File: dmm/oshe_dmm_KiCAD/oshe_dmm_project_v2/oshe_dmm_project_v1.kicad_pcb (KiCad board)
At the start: 4 copper layers, 88.7 x 165.1 mm, 99 parts, among them J1 FTDI Basic, J10 Voltage Range 2, J11 Voltage Range 3, J12 Voltage Range 3, J13 DC Current Indication, J14 Continuity, J16 AC Voltage Range 2, J18 AC Voltage Range 3, J2 Voltage, J20 AC Voltage Range 1, J21 AC Current Indication, J22 MJ-3536N, J3 GND, J4 Current, J5 Resistance Meas, J6 ON/OFF, J7 Voltage Range 1, J8 Voltage Range 1, J9 Voltage Range 2, SW1 PTS526 SK15 SMTR2 LFS, U1 ATmega328P-A, U2 AD736, U3 ADS1115IDGS, U4 MAX4617CPE, U5 LM317_SOT-223, U7 TPS60400DBV, U8 ADS1115IDGS, Y1 16MHz

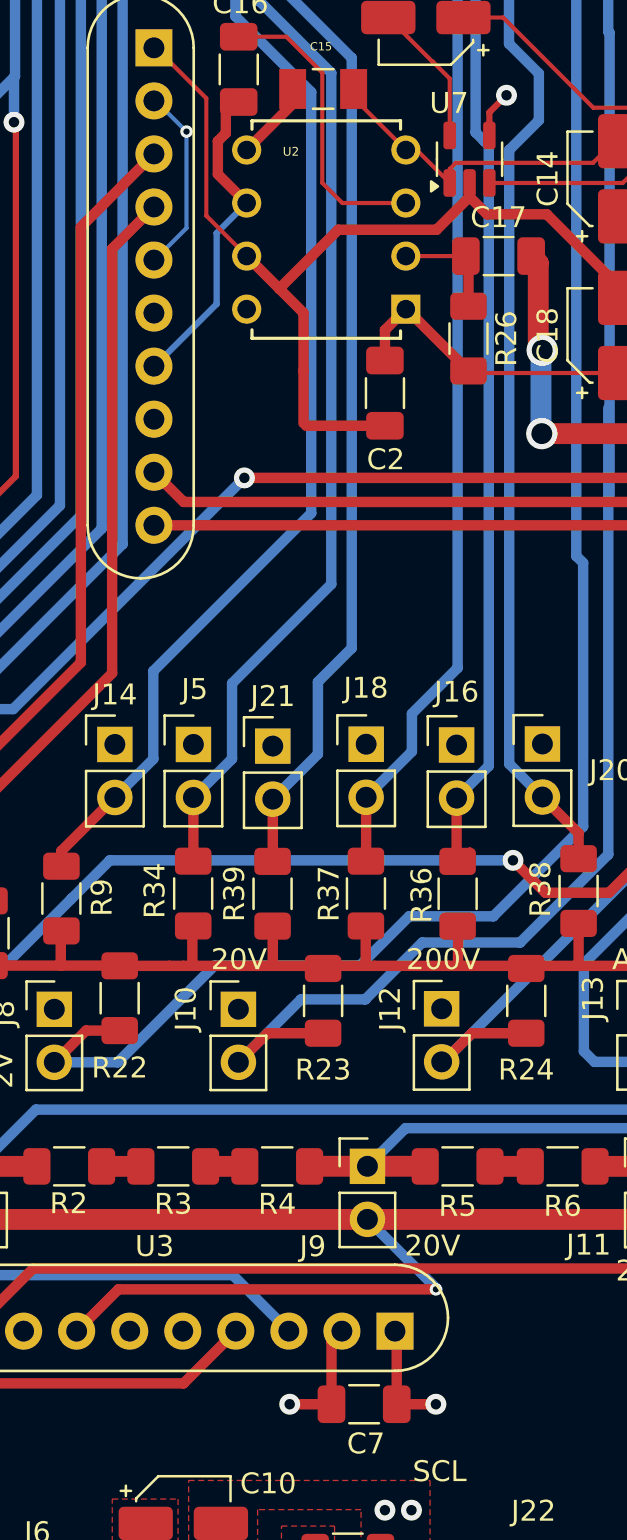
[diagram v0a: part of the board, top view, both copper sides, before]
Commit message: Removed buried vias
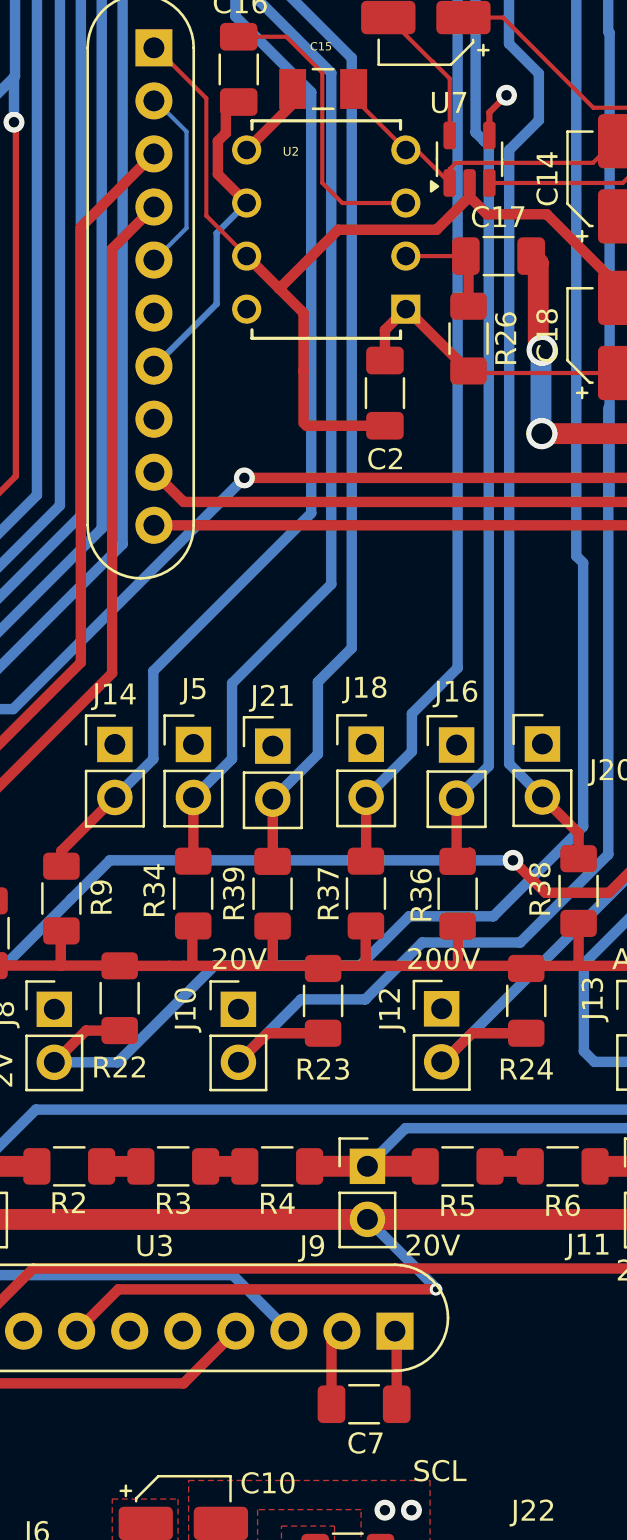
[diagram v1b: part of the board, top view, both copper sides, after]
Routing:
- net GND: track 88.7 -> 86.7 mm, vias 25 -> 23
- net +5V: track 162.8 -> 160.9 mm, vias 19 -> 18
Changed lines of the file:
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@@
-	)
-	(segment
-		(start 162.09 202.378)
-		(end 164.09 202.378)
-		(width 0.5)
-		(layer "F.Cu")
-		(net 2)
 	)
 	(segment
@@
 		(net 2)
 	)
-	(via blind
-		(at 162.09 202.378)
-		(size 1)
-		(drill 0.5)
-		(layers "F.Cu" "In1.Cu")
-		(free yes)
-		(net 2)
-	)
 	(via
 		(at 167.919 207.45)
@@
 		(net 2)
 	)
-	(via blind
-		(at 157.15 141.448)
-		(size 0.6)
-		(drill 0.3)
-		(layers "In1.Cu" "B.Cu")
-		(net 2)
-	)
 	(segment
 		(start 133.286 181.0106)
@@
 		(start 162.75 150.128)
 		(end 161.59 148.968)
-		(width 0.5)
-		(layer "F.Cu")
-		(net 4)
-	)
-	(segment
-		(start 169.09 202.378)
-		(end 167.215 202.378)
 		(width 0.5)
 		(layer "F.Cu")
@@
 		(free yes)
 		(net 4)
-	)
-	(via micro
-		(at 169.09 202.378)
-		(size 1)
-		(drill 0.5)
-		(layers "F.Cu" "In2.Cu")
-		(free yes)
-		(net 4)

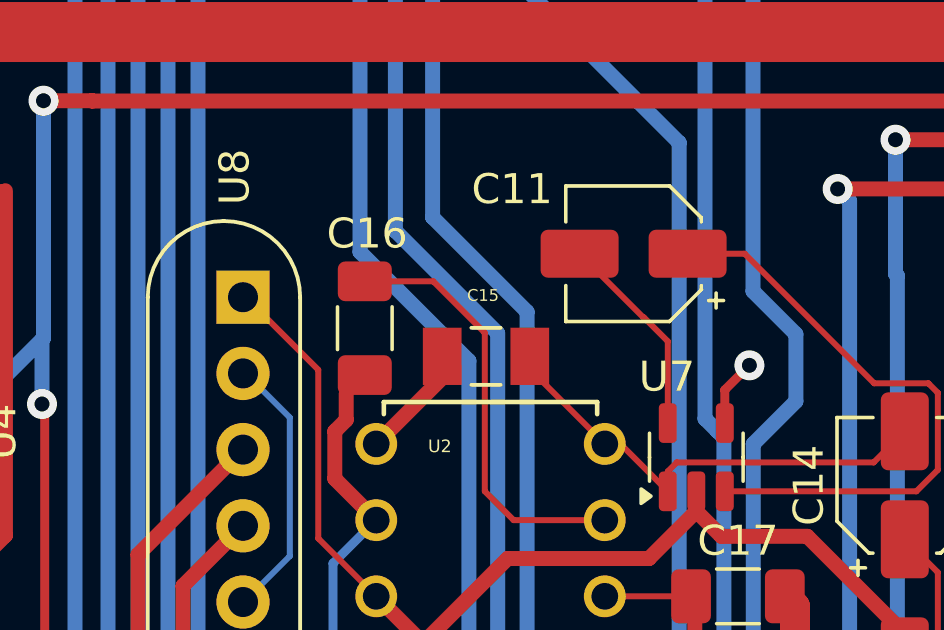
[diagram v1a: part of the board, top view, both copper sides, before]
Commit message: Removed a via
Removed a via that was incorrectly attached to multiple layers.
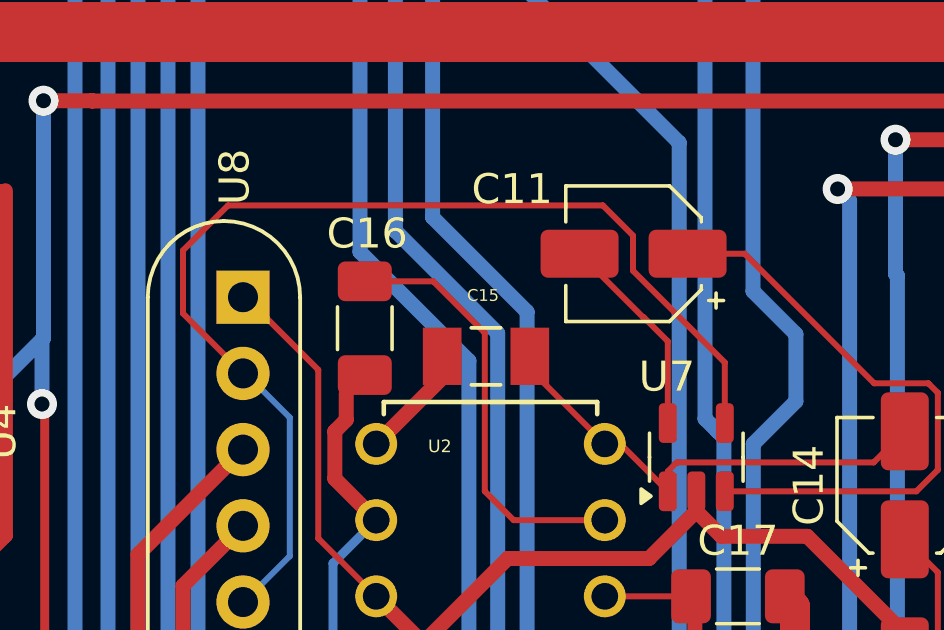
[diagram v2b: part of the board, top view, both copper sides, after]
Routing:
- net GND: track 86.7 -> 112.9 mm, vias 23 -> 22
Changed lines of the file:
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@@
+	)
+	(segment
+		(start 168.59 135.38184)
+		(end 167.58616 134.378)
+		(width 0.2)
+		(layer "F.Cu")
+		(net 2)
 	)
 	(segment
@@
 	)
 	(segment
+		(start 155.09 134.378)
+		(end 153.59 135.878)
+		(width 0.2)
+		(layer "F.Cu")
+		(net 2)
+	)
+	(segment
 		(start 133.286 172.5106)
 		(end 133.286 173.9476)
@@
 	)
 	(segment
+		(start 171.65 141.633)
+		(end 171.65 139.61416)
+		(width 0.2)
+		(layer "F.Cu")
+		(net 2)
+	)
+	(segment
+		(start 153.59 135.878)
+		(end 153.59 137.978)
+		(width 0.2)
+		(layer "F.Cu")
+		(net 2)
+	)
+	(segment
 		(start 135.699054 167.356146)
 		(end 135.699054 167.356054)
@@
 	)
 	(segment
-		(start 171.65 141.633)
-		(end 171.65 140.528)
-		(width 0.3)
-		(layer "F.Cu")
-		(net 2)
-	)
-	(segment
 		(start 127.2362 190.5378)
 		(end 126.144 191.63)
@@
 	)
 	(segment
-		(start 171.65 140.528)
-		(end 172.47 139.708)
-		(width 0.3)
-		(layer "F.Cu")
-		(net 2)
-	)
-	(segment
 		(start 134.067 174.7286)
 		(end 134.067 178.9196)
@@
 	)
 	(segment
+		(start 171.65 139.61416)
+		(end 168.59 136.55416)
+		(width 0.2)
+		(layer "F.Cu")
+		(net 2)
+	)
+	(segment
+		(start 168.59 136.55416)
+		(end 168.59 135.38184)
+		(width 0.2)
+		(layer "F.Cu")
+		(net 2)
+	)
+	(segment
 		(start 134.067 178.9196)
 		(end 134.086 178.9386)
@@
 	)
 	(segment
+		(start 167.58616 134.378)
+		(end 155.09 134.378)
+		(width 0.2)
+		(layer "F.Cu")
+		(net 2)
+	)
+	(segment
 		(start 177.65 153.008)
 		(end 170.75 153.008)
@@
 		(end 135.083 184.6346)
 		(width 0.3)
+		(layer "F.Cu")
+		(net 2)
+	)
+	(segment
+		(start 153.59 137.978)
+		(end 155.59 139.978)
+		(width 0.2)
 		(layer "F.Cu")
 		(net 2)
@@
 		(net 2)
 	)
-	(via
-		(at 172.47 139.708)
-		(size 1)
-		(drill 0.5)
-		(layers "F.Cu" "B.Cu")
-		(net 2)
-	)

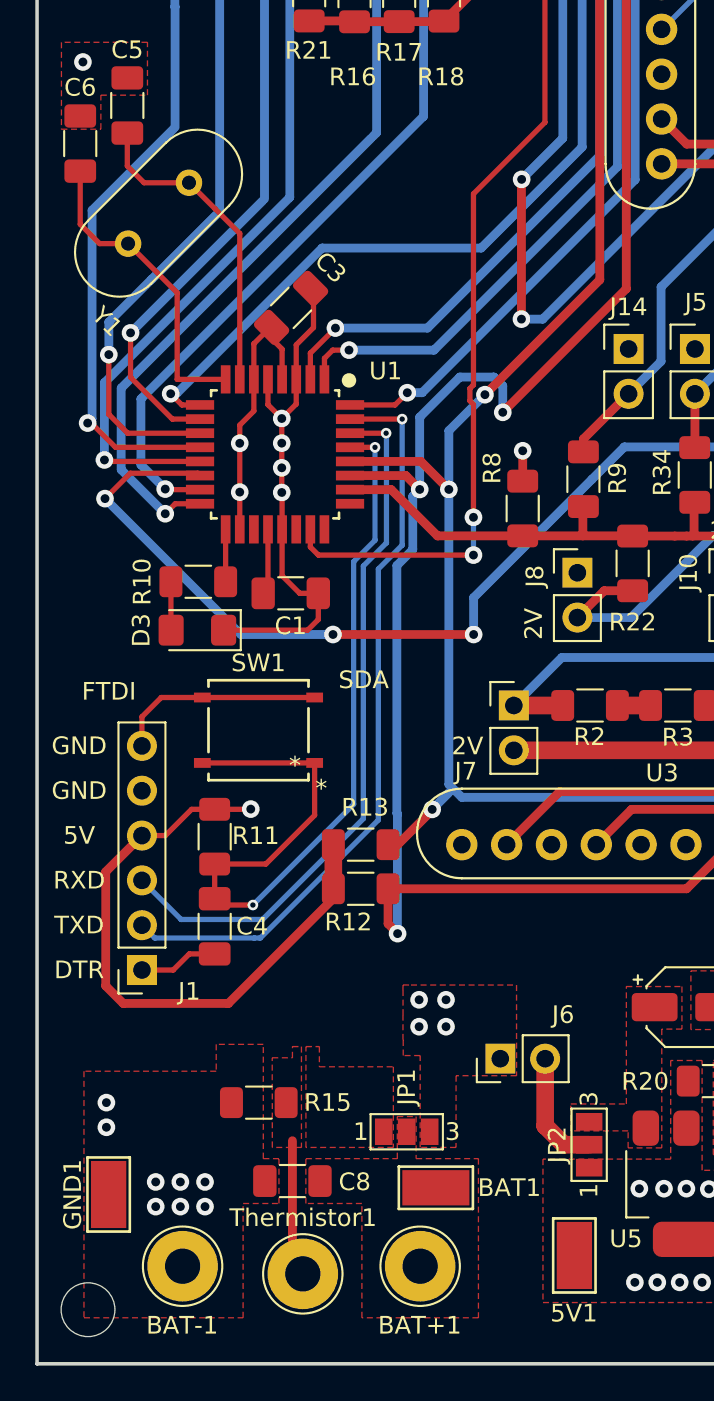
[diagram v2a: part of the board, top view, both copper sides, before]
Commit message: Last minute changes
Added header pins to make boot loading easier, removed battery management circuit for the rechargeable version, fixed i2c address pin that was connected to GND instead of 5V.
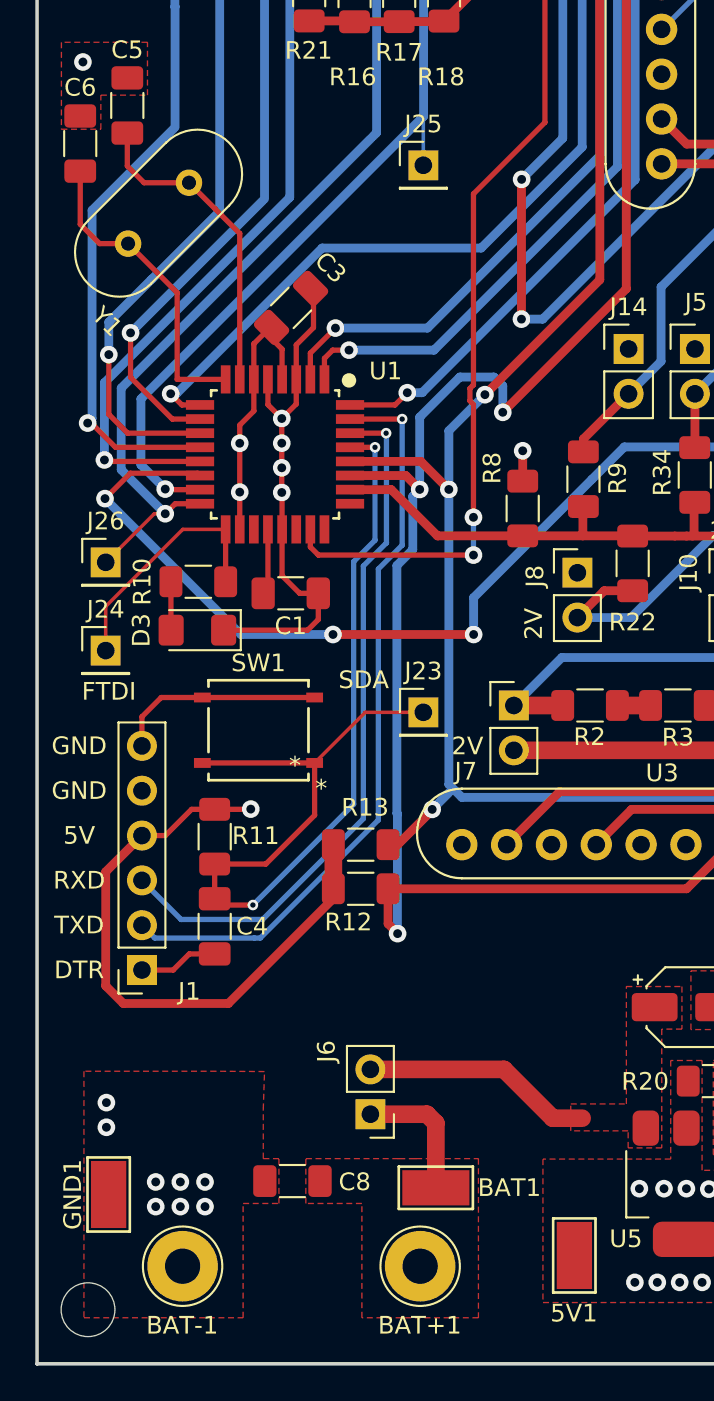
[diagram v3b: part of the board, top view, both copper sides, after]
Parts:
- removed JP1, JP2: SolderJumper, Jumper:SolderJumper-3_P1.3mm_Open_Pad1.0x1.5mm_NumberLabels
- removed R15: 10k, Resistor_SMD:R_1206_3216Metric_Pad1.30x1.75mm_HandSolder
- removed Thermistor1: Pad, TestPoint:TestPoint_THTPad_D4.0mm_Drill2.0mm
- added J23: Reset, Connector_PinHeader_2.54mm:PinHeader_1x01_P2.54mm_Vertical, F.Cu at (142.1, 191.4)
- added J24: D13, Connector_PinHeader_2.54mm:PinHeader_1x01_P2.54mm_Vertical, F.Cu at (124.1, 187.9)
- added J25: D11, Connector_PinHeader_2.54mm:PinHeader_1x01_P2.54mm_Vertical, F.Cu at (142.1, 160.4)
- added J26: D12, Connector_PinHeader_2.54mm:PinHeader_1x01_P2.54mm_Vertical, F.Cu at (124.1, 182.9)
- moved J6 8.01 mm to (139.1, 214.2), turned to 180 degrees
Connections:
- BAT+1 pad 1: Net-(JP1-C) -> BMS_Power_Out
- BAT1 pad 1: Net-(JP1-C) -> BMS_Power_Out
- C10 pad 1: Net-(JP2-B) -> Net-(J6-Pin_2)
- C8 pad 1: Net-(JP1-C) -> BMS_Power_Out
- J6 pad 1: 9V_BAT_IN -> BMS_Power_Out
- U3 pad 2: GND -> +5V
- U3 pad 5: GND -> +5V
- U5 pad 3: Net-(JP2-B) -> Net-(J6-Pin_2)
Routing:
- net SCK/D13: track 3.38 -> 14.5 mm
- net TS: track 7.79 -> 0.00 mm
- net BMS_Power_Out: track 0.00 -> 7.58 mm
- net Net-(J23-Pin_1): track 50.6 -> 58.0 mm
- net Net-(J6-Pin_2): track 6.74 -> 13.2 mm
- net MISO/D12: track 115.5 -> 120.0 mm
- net MOSI/D11: track 115.0 -> 117.7 mm
- net 9V_BAT_IN: vias 4 -> 0
- added copper zone on F.Cu, net BMS_Power_Out
- added copper zone on F.Cu, net Net-(J6-Pin_2)
- removed copper zone on F.Cu, net 9V_BAT_IN
- removed copper zone on F.Cu, net BMS_BAT_IN
- removed copper zone on F.Cu, net Net-(JP1-C)
- removed copper zone on F.Cu, net Net-(JP2-B)
- removed copper zone on F.Cu, net TS

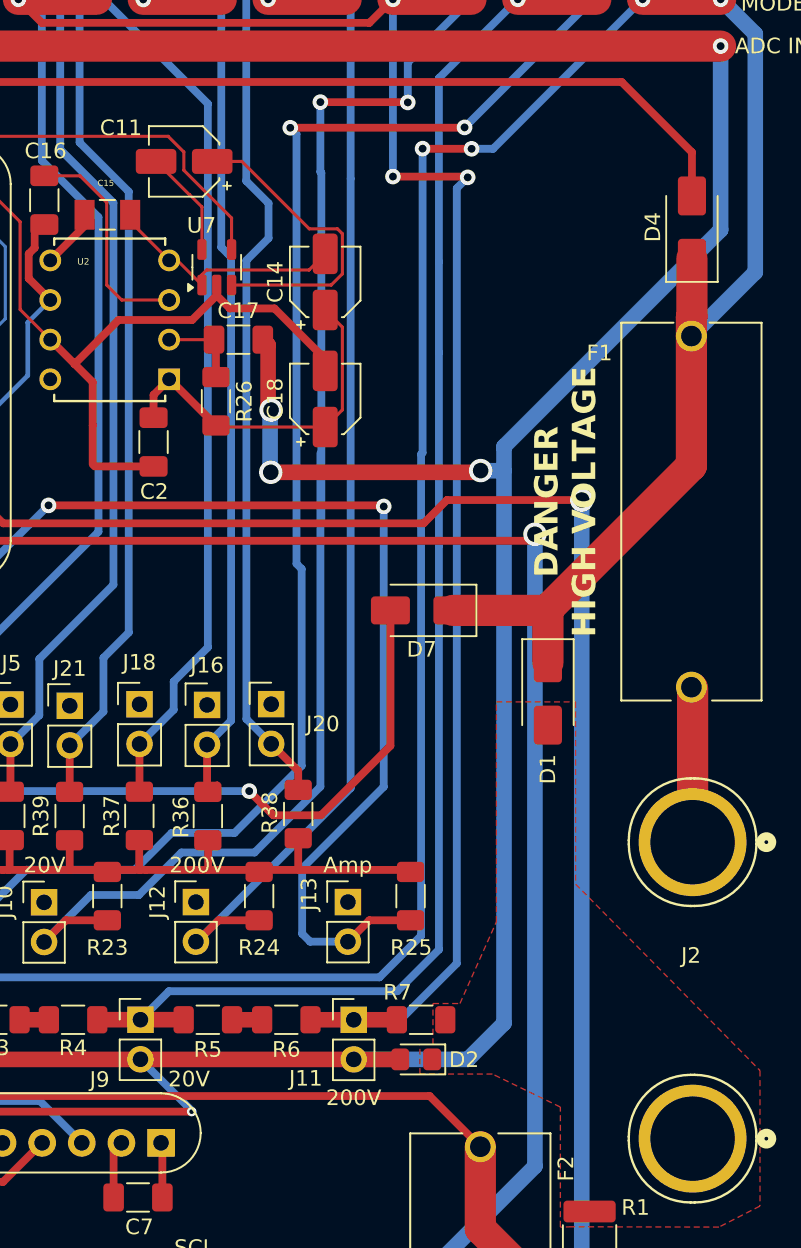
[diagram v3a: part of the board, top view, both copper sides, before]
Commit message: Added New Input Probe
Added a new input probe for resistance measurement. Also fixed the direction of some polarized capacitors.
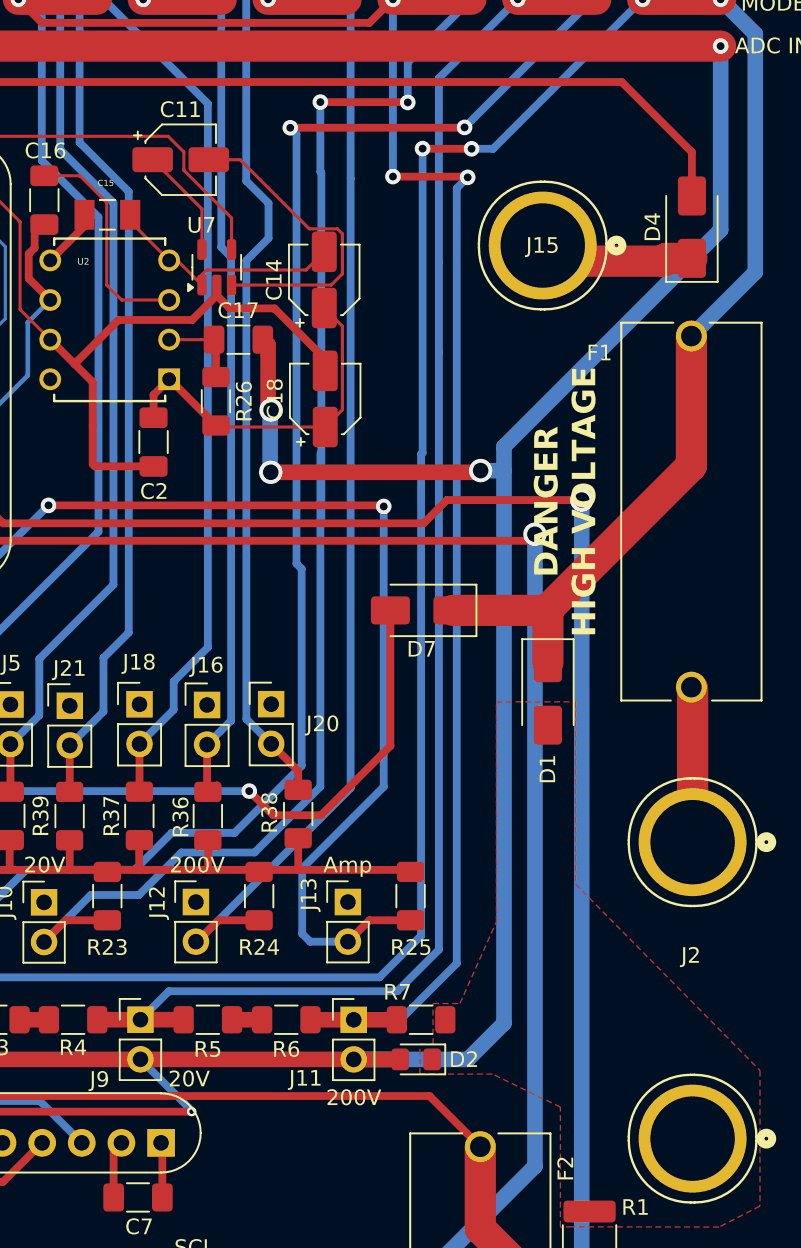
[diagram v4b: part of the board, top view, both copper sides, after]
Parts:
- added J15: Resistance, DMM_Footprint_Library:CONN_575-8_KEY, F.Cu at (191.6, 141.4)
- moved C11 0.25 mm to (168.4, 135.9), turned to 0 degrees
- moved C14 0.14 mm to (177.6, 143.6)
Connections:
- net BMS_Power_Out renamed Net-(J6-Pin_1)
- C11 pad 1: Net-(U7-C_{FLY-}) -> Net-(U7-C_{FLY+})
- C11 pad 2: Net-(U7-C_{FLY+}) -> Net-(U7-C_{FLY-})
- D4 pad 1: 2V_Rang -> Resistance_Input
- U3 pad 2: +5V -> GND
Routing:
- net Resistance_Input: track 0.00 -> 10.0 mm
- net 2V_Rang: track 202.4 -> 197.5 mm
